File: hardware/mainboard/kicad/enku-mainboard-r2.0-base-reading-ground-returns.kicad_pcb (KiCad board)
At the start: 4 copper layers, 59 x 101 mm, 132 parts, among them J1 1S LiPo + NTC, J2 Hirose DM3AT-SF-PEJM5, J3 FH34SRJ-24S-0.5SH(50), J5 GCT USB4105-GF-A-120, J6 4-pin pogo dock, J7 Tag-Connect TC2030-IDC-NL, Q1 IRLML6346TRPBF, Q2 AO3401A, SW1 HARD POWER, SW2 BOOT / RECOVERY, SW3 BTN_L1, SW4 BTN_L2, SW5 BTN_R1, SW6 BTN_R2, U1 ESP32-S3-WROOM-1-N16R8, U10 TLV3012BIDBVR, U2 TPS2121, U3 BQ25185DLHR, U4 TPS63802DLAR, U5 BMI270, U8 USBLC6-2SC6, U9 TMUX1101DBVR

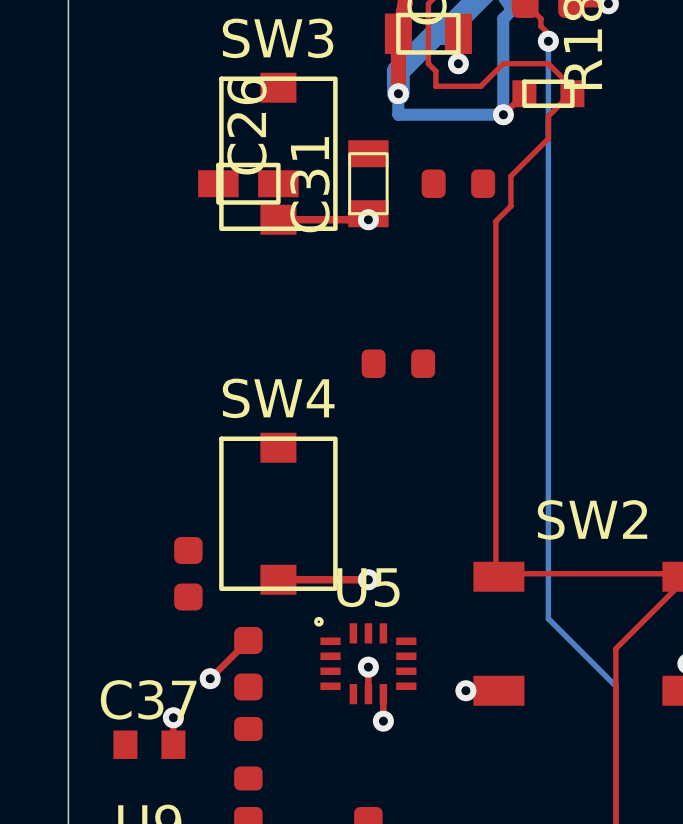
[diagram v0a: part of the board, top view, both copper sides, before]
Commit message: R43: join local C26 EPD bypass and C18/C19 IMU bulk GND to reading button plane returns
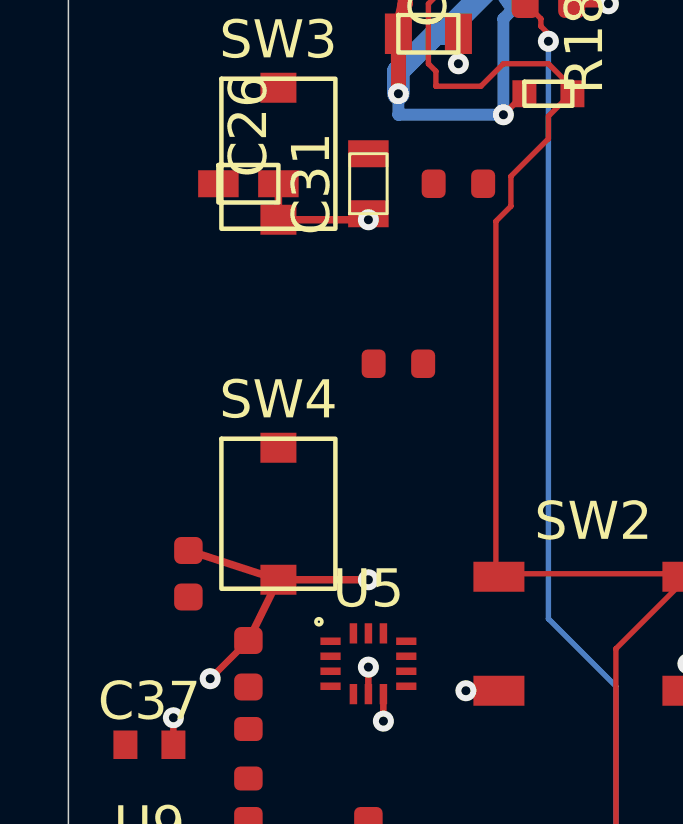
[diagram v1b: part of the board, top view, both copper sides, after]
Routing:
- net GND: track 105.1 -> 111.7 mm
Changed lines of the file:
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@@
   (segment (start 71.2 77.2) (end 68 77.2) (width 0.25) (layer "F.Cu") (net 1))
   (via (at 68 77.2) (size 0.70) (drill 0.30) (layers "F.Cu" "B.Cu") (net 1))
+  (segment (start 25 65.2) (end 25 64) (width 0.25) (layer "F.Cu") (net 1))
+  (segment (start 25 77.2) (end 22 76.225) (width 0.25) (layer "F.Cu") (net 1))
+  (segment (start 25 77.2) (end 24 79.225) (width 0.25) (layer "F.Cu") (net 1))
 )
